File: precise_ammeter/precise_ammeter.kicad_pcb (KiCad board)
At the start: 2 copper layers, 70 x 80 mm, 103 parts, among them J1 Conn_01x01_Socket, J2 Conn_01x01_Socket, J3 USB4110GFA, J4 Conn_ARM_JTAG_SWD_10, J5 XT30_Male, J6 Conn_01x04_Socket, U1 INA121U, U10 TPS7A2450DBVR, U11 STM32G431C6Tx, U12 USBLC6-2P6, U2 TLV9301xDBV, U3 TLV9301xDBV, U4 INA137UA, U5 OPA376xxD, U6 OPA376xxD, U7 TPS7A2433DBVR, U8 TPS7A2450DBVR, U9 LMC7660, Y1 Crystal 8MHz

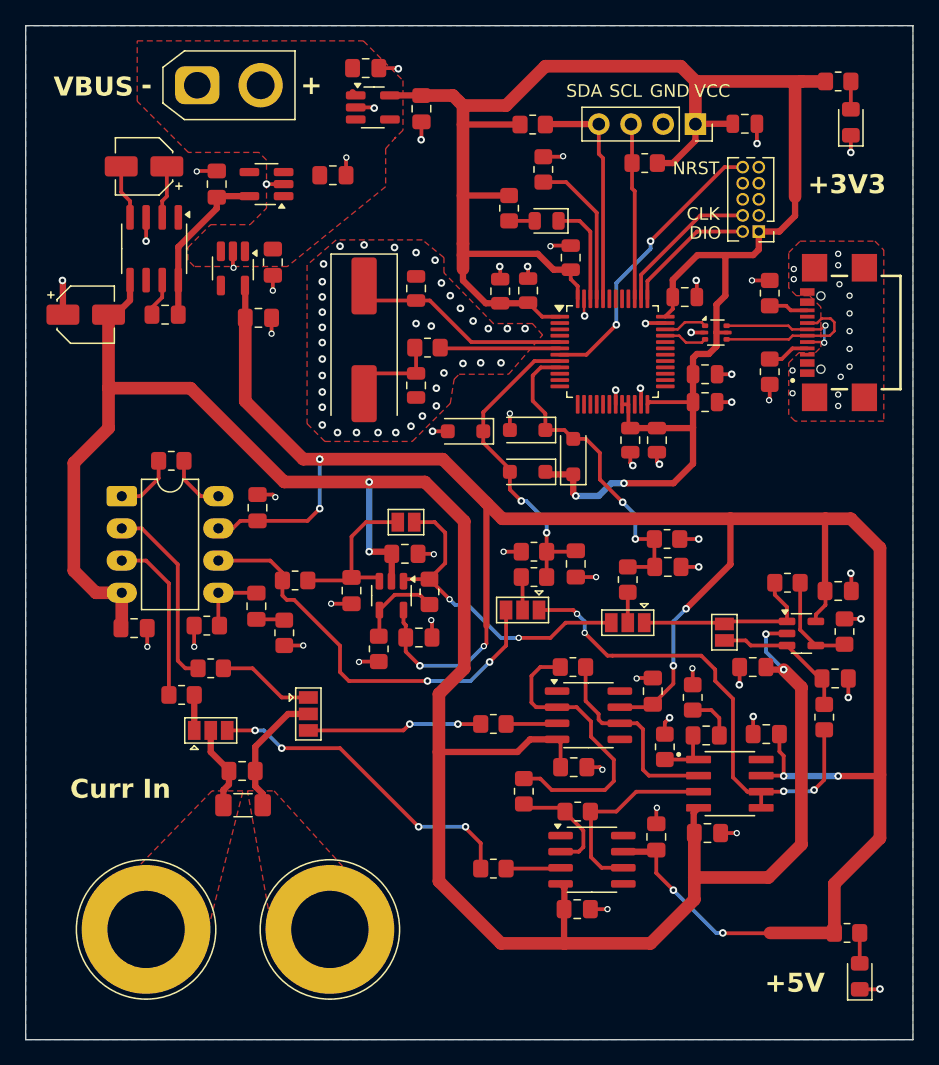
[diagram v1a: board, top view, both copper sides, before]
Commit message: przesunieto konektory LCD i SWD. Przesunieto diode LED 3v3
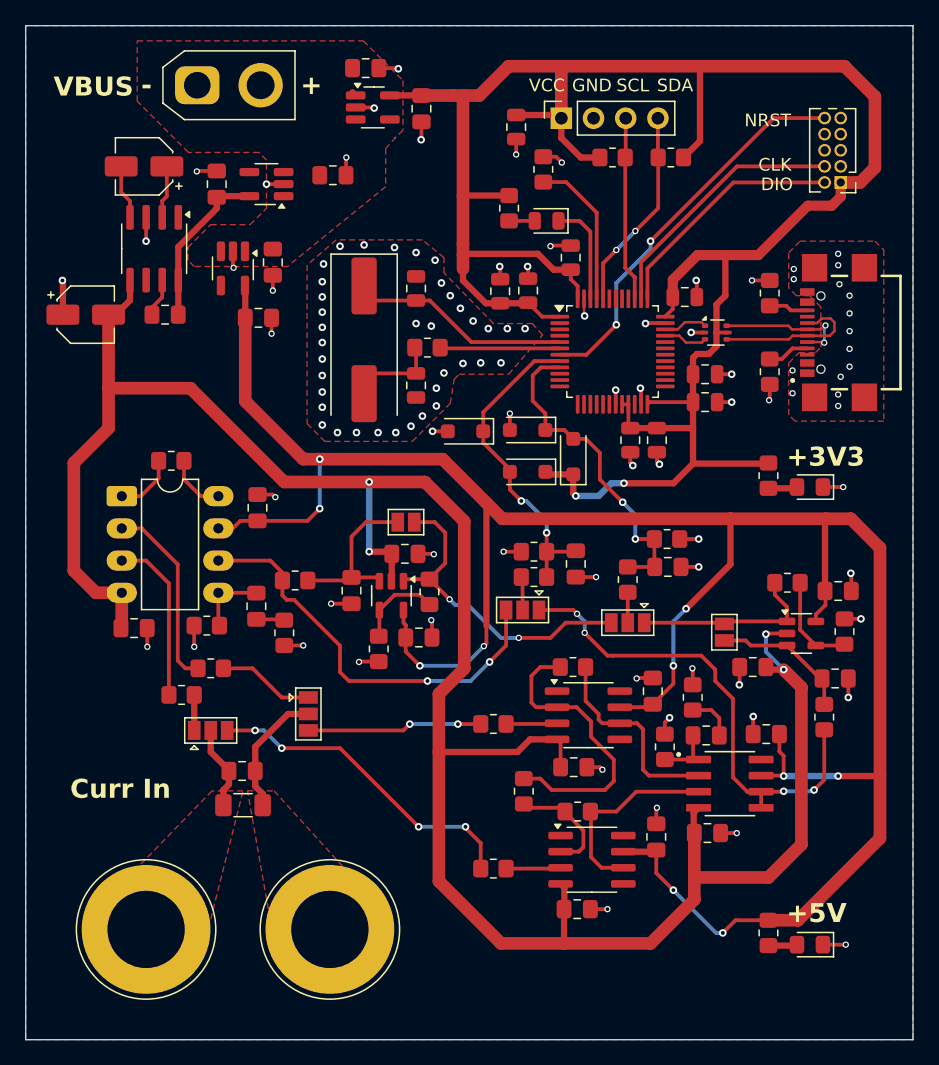
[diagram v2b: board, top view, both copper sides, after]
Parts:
- moved R26 31.6 mm to (233.1, 84.5), turned to -90 degrees
- moved D2 29.0 mm to (236.4, 85.4), turned to 180 degrees
- moved C40 18.0 mm to (213.2, 57.0), turned to -90 degrees
- moved R31 11.2 mm to (225.4, 59.4), turned to 0 degrees
- moved J6 10.6 mm to (216.8, 56.3), turned to 90 degrees
- moved J4 7.53 mm to (238.8, 61.4)
- moved R27 6.20 mm to (233.1, 120.6), turned to -90 degrees
- moved D1 4.65 mm to (236.4, 121.5), turned to 180 degrees
- moved R30 2.58 mm to (220.8, 59.4), turned to 180 degrees
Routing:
- net +3V3: track 162.1 -> 180.8 mm
- net /MCU/SWDIO: track 10.5 -> 19.2 mm
- net /MCU/SWCLK: track 11.9 -> 20.5 mm
- net /MCU/NRST: track 22.8 -> 30.9 mm
- net +5VA: track 192.0 -> 189.8 mm
- net /MCU/SDA: track 18.2 -> 16.1 mm, vias 0 -> 2
- net /MCU/SCL: track 13.9 -> 14.6 mm
